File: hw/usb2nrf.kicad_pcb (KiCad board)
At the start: 2 copper layers, 24.9 x 26.3 mm, 16 parts, among them IC1 ATMEGA8-AI, P1 CONN_01X03, P2 CONN_01X02, P3 CONN_01X06, P4 USBTTL, Y1 Crystal

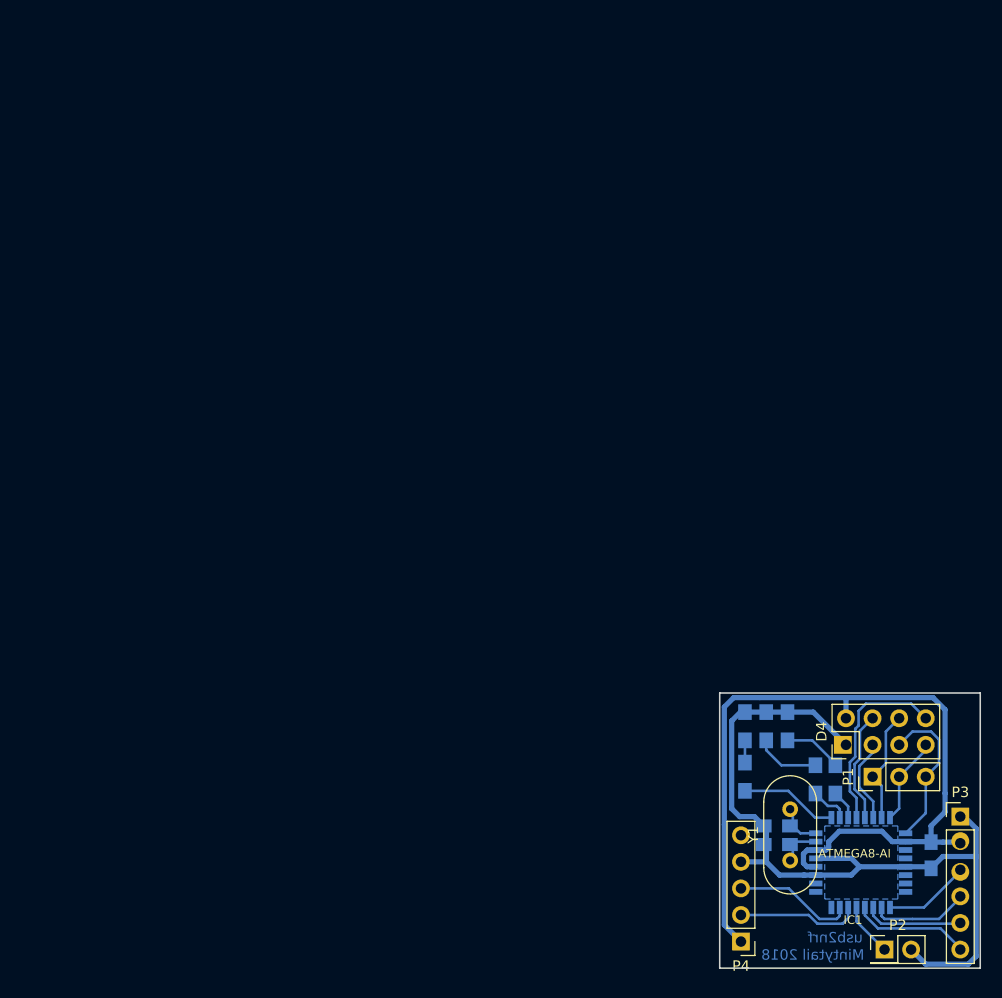
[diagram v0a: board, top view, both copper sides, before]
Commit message: hw: update kicad version
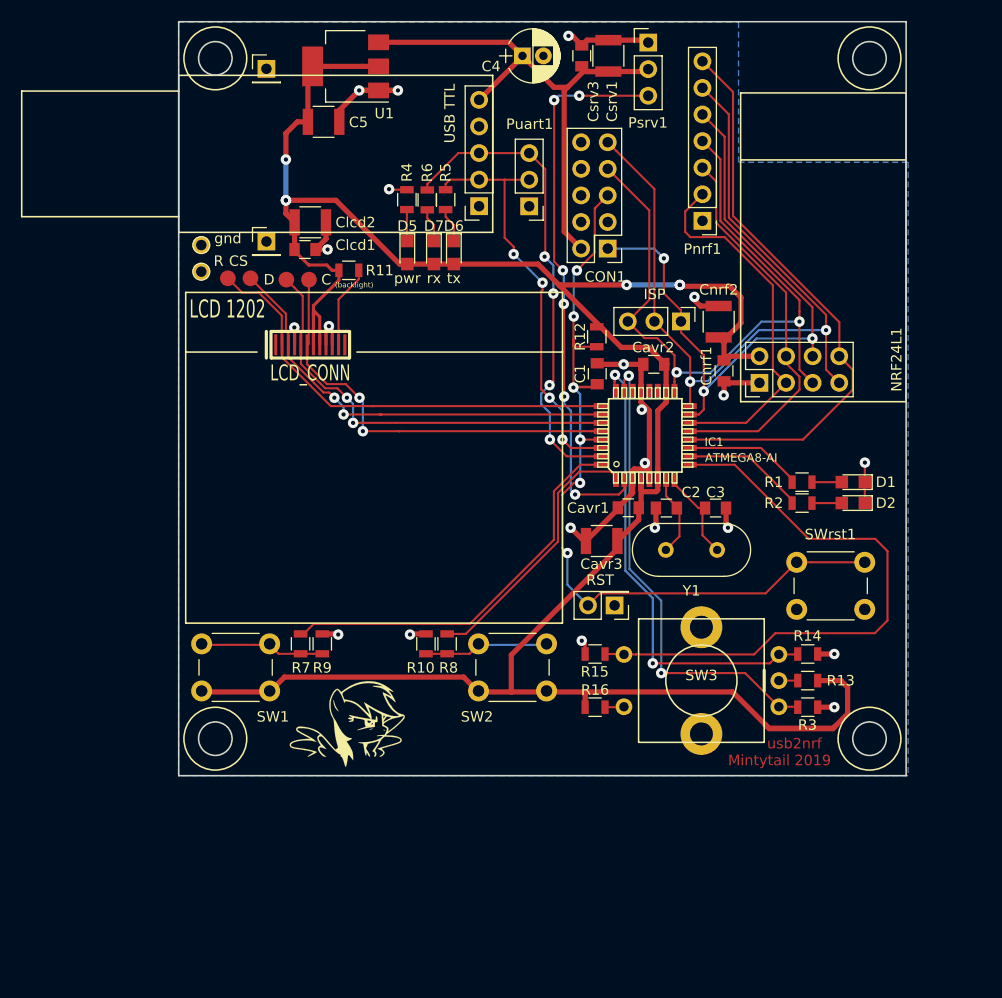
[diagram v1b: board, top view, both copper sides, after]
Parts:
- removed D3: LED, LEDs:LED_0805_HandSoldering
- removed D4: NRF24L01, Pin_Headers:Pin_Header_Straight_2x04_Pitch2.54mm
- removed P4: USBTTL, Pin_Headers:Pin_Header_Straight_1x05_Pitch2.54mm
- added C: Measurement_Point_Round-SMD-Pad_Small, Measurement_Points:Measurement_Point_Round-SMD-Pad_Small, F.Cu at (117.6, 70.0)
- added C4: 10u, Capacitors_ThroughHole:CP_Radial_D5.0mm_P2.00mm, F.Cu at (138.0, 48.6)
- added C5: 10u, Capacitors_SMD:C_1210, F.Cu at (119.0, 54.9)
- added CON1: AVR-JTAG-10, Pin_Headers:Pin_Header_Straight_2x05_Pitch2.54mm, F.Cu at (146.1, 67.0)
- added CS: Measurement_Point_Round-SMD-Pad_Small, Measurement_Points:Measurement_Point_Round-SMD-Pad_Small, F.Cu at (112.0, 69.8)
- added Cavr1: 100n, Capacitors_SMD:C_0805, F.Cu at (148.1, 91.8)
- added Cavr2: 100n, Capacitors_SMD:C_0805, F.Cu at (150.5, 78.1)
- added Cavr3: 10u, Capacitors_SMD:C_1210, F.Cu at (145.6, 95.0)
- added Clcd1: 100n, Capacitors_SMD:C_0805, F.Cu at (117.2, 67.1)
- added Clcd2: 10u, Capacitors_SMD:C_1210, F.Cu at (117.7, 64.5)
- added Cnrf1: 100n, Capacitors_SMD:C_0805, F.Cu at (157.3, 78.7)
- added Cnrf2: 10u, Capacitors_SMD:C_1210, F.Cu at (156.7, 74.0)
- added Csrv1: 10u, Capacitors_SMD:C_1210, F.Cu at (146.2, 48.6)
- added Csrv3: 100n, Capacitors_SMD:C_0805, F.Cu at (143.7, 48.6)
- added D: Measurement_Point_Round-SMD-Pad_Small, Measurement_Points:Measurement_Point_Round-SMD-Pad_Small, F.Cu at (115.4, 70.0)
- added D5: LED, LEDs:LED_0805, F.Cu at (127.0, 67.4)
- added D6: LED, LEDs:LED_0805, F.Cu at (131.4, 67.4)
- added D7: LED, LEDs:LED_0805, F.Cu at (129.5, 67.4)
- added G***: LOGO, hw:RD keeper, F.Cu at (120.8, 114.6)
- added LCD 1202: LCD_CONN, lcd_n1202:SIL-12, F.Cu at (115.8, 76.2)
- added NRF24L1: NRF24L01, Pin_Headers:Pin_Header_Straight_2x04_Pitch2.54mm, F.Cu at (160.6, 79.8)
- added P6: CONN_01X01, Pin_Headers:Pin_Header_Straight_1x01_Pitch2.54mm, F.Cu at (113.5, 66.3)
- added Pnrf1: nrf_test, Pin_Headers:Pin_Header_Straight_1x07_Pitch2.54mm, F.Cu at (155.2, 64.4)
- added Psrv1: CONN_srv, Pin_Headers:Pin_Header_Straight_1x03_Pitch2.54mm, F.Cu at (150.0, 47.3)
- added Puart1: uart_test, Pin_Headers:Pin_Header_Straight_1x03_Pitch2.54mm, F.Cu at (138.6, 63.0)
- added R: Measurement_Point_Round-SMD-Pad_Small, Measurement_Points:Measurement_Point_Round-SMD-Pad_Small, F.Cu at (109.9, 69.8)
- added R10: 10k, Resistors_SMD:R_0805, F.Cu at (128.8, 104.8)
- added R11: R, Resistors_SMD:R_0805, F.Cu at (121.4, 69.1)
- added R12: 47k, Resistors_SMD:R_0805, F.Cu at (145.1, 75.4)
- added R13: 511, Resistors_SMD:R_0805, F.Cu at (165.3, 108.3)
- added R14: 10k, Resistors_SMD:R_0805, F.Cu at (165.3, 105.7)
- added R15: 10k, Resistors_SMD:R_0805, F.Cu at (144.9, 105.7)
- added R16: 511, Resistors_SMD:R_0805, F.Cu at (144.9, 110.8)
- added R4: R, Resistors_SMD:R_0805, F.Cu at (127.0, 62.3)
- added R5: R, Resistors_SMD:R_0805, F.Cu at (130.7, 62.3)
- added R6: R, Resistors_SMD:R_0805, F.Cu at (128.9, 62.4)
- added R7: 150, Resistors_SMD:R_0805, F.Cu at (116.8, 104.8)
- added R8: 150, Resistors_SMD:R_0805, F.Cu at (130.8, 104.8)
- added R9: 10k, Resistors_SMD:R_0805, F.Cu at (118.9, 104.8)
- added REF**: PINTST, Connect:PINTST, F.Cu at (107.3, 66.7)
- added SW1: SW_Push, Buttons_Switches_ThroughHole:SW_PUSH_6mm_h4.3mm, F.Cu at (107.3, 104.8)
- added SW2: SW_Push, Buttons_Switches_ThroughHole:SW_PUSH_6mm_h4.3mm, F.Cu at (133.8, 104.8)
- added SW3: Rotary_Encoder_Switch, misc:encoder, F.Cu at (155.1, 108.3)
- added SWrst1: SW_Push, Buttons_Switches_ThroughHole:SW_PUSH_6mm_h4.3mm, F.Cu at (164.2, 97.0)
- added U1: AMS1117-3.3, TO_SOT_Packages_SMD:SOT-223-3_TabPin2, F.Cu at (121.1, 49.6)
- added USB TTL: USBTTL, Pin_Headers:Pin_Header_Straight_1x05_Pitch2.54mm, F.Cu at (133.9, 62.9)
- added gnd: PINTST, Connect:PINTST, F.Cu at (107.3, 69.2)
- C1: footprint Capacitors_SMD:C_0805_HandSoldering -> Capacitors_SMD:C_0805; moved to F.Cu
- C2, C3: value C -> 22p; footprint Capacitors_SMD:C_0805_HandSoldering -> Capacitors_SMD:C_0805; moved to F.Cu
- D1, D2: footprint LEDs:LED_0805_HandSoldering -> LEDs:LED_0805; moved to F.Cu
- IC1: moved to F.Cu
- P3: value CONN_01X06 -> CONN_01X01; footprint Pin_Headers:Pin_Header_Straight_1x06_Pitch2.54mm -> Pin_Headers:Pin_Header_Straight_1x01_Pitch2.54mm
- R1, R2: footprint Resistors_SMD:R_0805_HandSoldering -> Resistors_SMD:R_0805; moved to F.Cu
- R3: value R -> 10k; footprint Resistors_SMD:R_0805_HandSoldering -> Resistors_SMD:R_0805; moved to F.Cu
- Y1: value Crystal -> 16M
- moved P3 97.5 mm to (113.5, 49.8)
- moved C1 56.0 mm to (145.1, 79.0), turned to 90 degrees
- moved ISP 47.2 mm to (153.1, 74.0), turned to 270 degrees
- moved IC1 45.7 mm to (149.7, 84.9), turned to 90 degrees
- moved RST 41.8 mm to (146.8, 101.1), turned to 180 degrees
- moved C2 33.8 mm to (151.8, 91.8)
- moved Y1 32.0 mm to (151.7, 95.8), turned to 0 degrees
- moved C3 30.9 mm to (156.4, 91.8), turned to 0 degrees
- moved R1 28.6 mm to (164.7, 89.3), turned to 0 degrees
- moved R2 26.4 mm to (164.7, 91.3), turned to 0 degrees
- moved D1 24.2 mm to (169.6, 89.3), turned to 180 degrees
- moved D2 22.9 mm to (169.6, 91.3), turned to 180 degrees
- moved R3 8.95 mm to (165.3, 110.8), turned to 0 degrees
- renumbered P1 to ISP, P2 to RST
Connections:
- C1 pad 1: /3v3 -> /reset
- C1 pad 2: /gnd -> GNDPWR
- C2 pad 2: /gnd -> GNDPWR
- C3 pad 2: /gnd -> GNDPWR
- D1 pad 1: /gnd -> GNDPWR
- D2 pad 1: /gnd -> GNDPWR
- IC1 pad 21: /gnd -> GNDPWR
- IC1 pad 3: /gnd -> GNDPWR
- IC1 pad 5: /gnd -> GNDPWR
- IC1 pad 9: Net-(IC1-Pad9) -> /enc_btn
- P3 pad 1: /gnd -> GNDPWR
- R3 pad 1: Net-(IC1-Pad9) -> Net-(IC1-Pad23)
- R3 pad 2: Net-(D3-Pad2) -> GNDPWR
- RST pad 1: /reset -> GNDPWR
- RST pad 2: /gnd -> /reset
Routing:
- net /3v3: track 79.5 -> 254.8 mm, vias 0 -> 6
- net GNDPWR: track 0.00 -> 86.0 mm, vias 0 -> 21
- net /reset: track 5.13 -> 85.5 mm, vias 0 -> 6
- net /gnd: track 78.9 -> 0.00 mm
- net /miso: track 8.37 -> 77.1 mm, vias 0 -> 2
- net /enc_btn: track 0.00 -> 57.3 mm
- net /5v: track 0.00 -> 53.8 mm
- net Net-(IC1-Pad2): track 0.00 -> 53.4 mm, vias 0 -> 6
- net /sck: track 14.9 -> 67.9 mm, vias 0 -> 2
- net /mosi: track 10.9 -> 63.2 mm, vias 0 -> 3
- net Net-(IC1-Pad23): track 0.00 -> 45.7 mm, vias 0 -> 2
- net Net-(IC1-Pad24): track 0.00 -> 44.8 mm, vias 0 -> 2
- net Net-(IC1-Pad32): track 0.00 -> 38.1 mm
- net /irq: track 18.1 -> 54.8 mm
- net /lcd_rst: track 8.34 -> 43.1 mm
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- added copper zone on B.Cu, net GNDPWR
- removed copper zone on B.Cu, net /gnd
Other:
- board size 24.9 x 26.3 mm -> 69.5 x 72 mm
- net class Default: trace_width 0.25 -> 0.2; via_dia 1.7 -> 1; via_drill 1 -> 0.4
- net class power: via_dia 1.7 -> 1; via_drill 1 -> 0.4
- net class thin power added: clearance 0.2, trace_width 0.3, via_dia 1, via_drill 0.4
- rule trace_min: 0.2 -> 0.15
- board text added: "(backlight)"
- board text added: "Mintytail 2019"
- board text added: "pwr"
- board text added: "rx"
- board text added: "tx"
- board text removed: "Mintytail 2018"
